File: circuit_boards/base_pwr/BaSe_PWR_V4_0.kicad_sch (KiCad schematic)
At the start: 107 parts, among them J1 12VDC In, J1 USB_C_Receptacle, J10 Conn_01x04_Socket, J11 MOTOR, J3 USB3_A, J3 USB_B_Micro, J4 Conn_01x07_Pin, J5 Conn_02x06_Odd_Even, J7 Conn_02x06_Odd_Even, J7 USB3_B_Micro, J9 Conn_01x04_Socket, P1 USB_C_Plug, Q1 AOSP21321, Q2 BSS214NW, Q3 BSS214NW, Q4 BSS214NW, Q5 BSS214NW, U1 STM32F070RBTx, U2 LM2596S-5, U3 AMS1117-3.3, U4 AMS1117-3.3, U5 DRV8220, U6 TS0101F020V4, Y1 8MHz

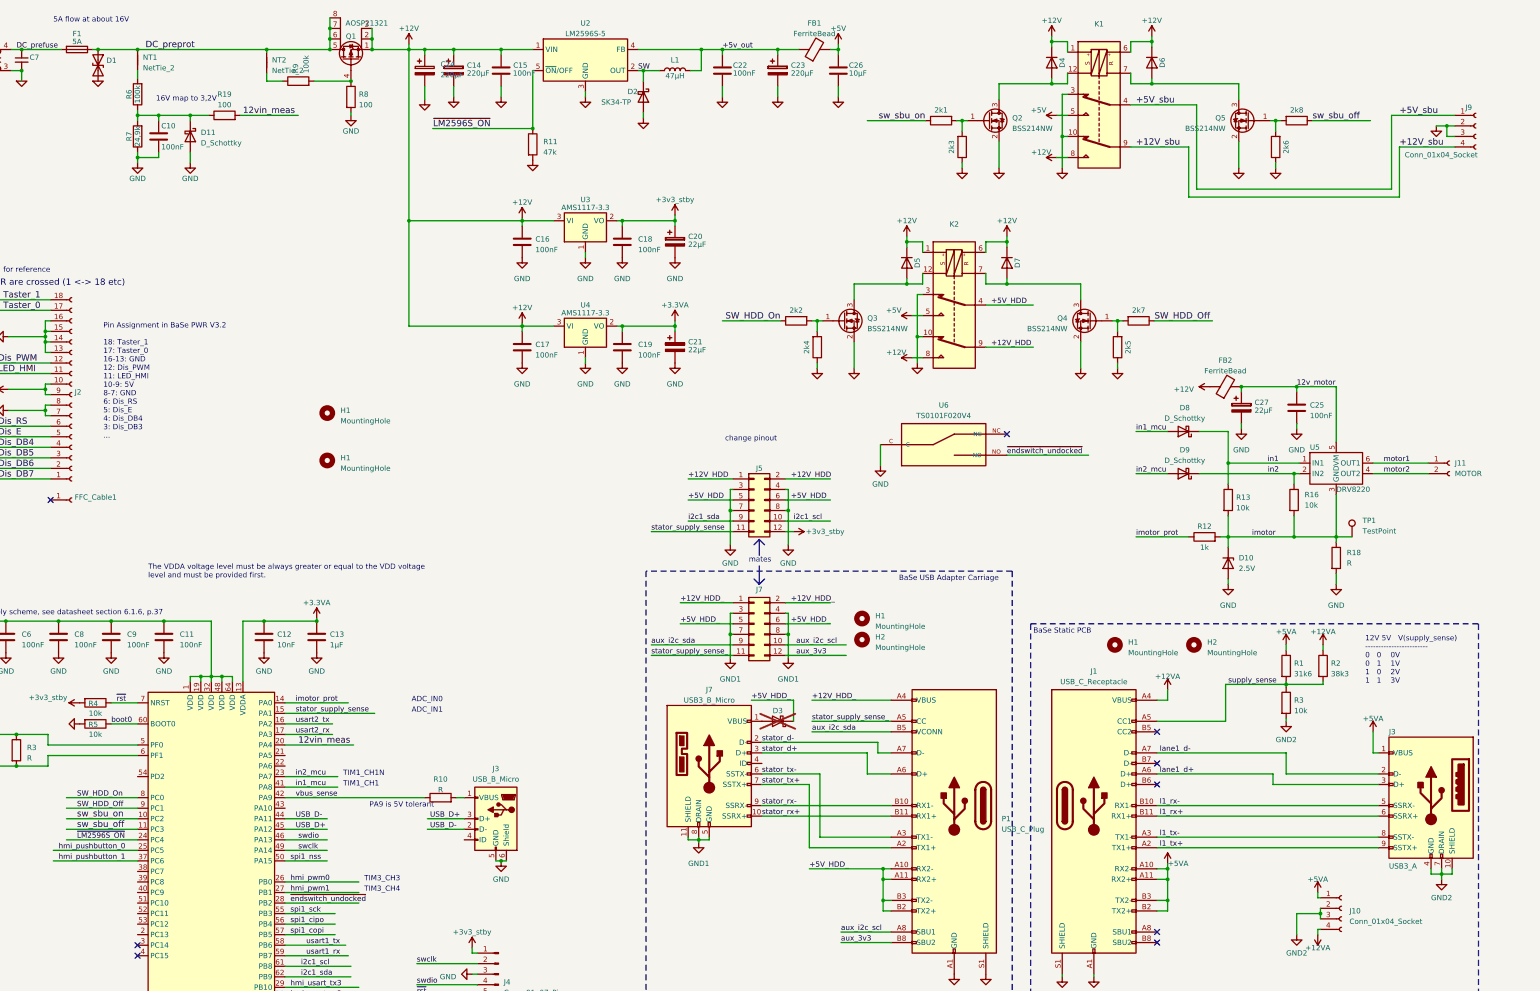
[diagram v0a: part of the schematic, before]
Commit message: update resistor values for supply sense
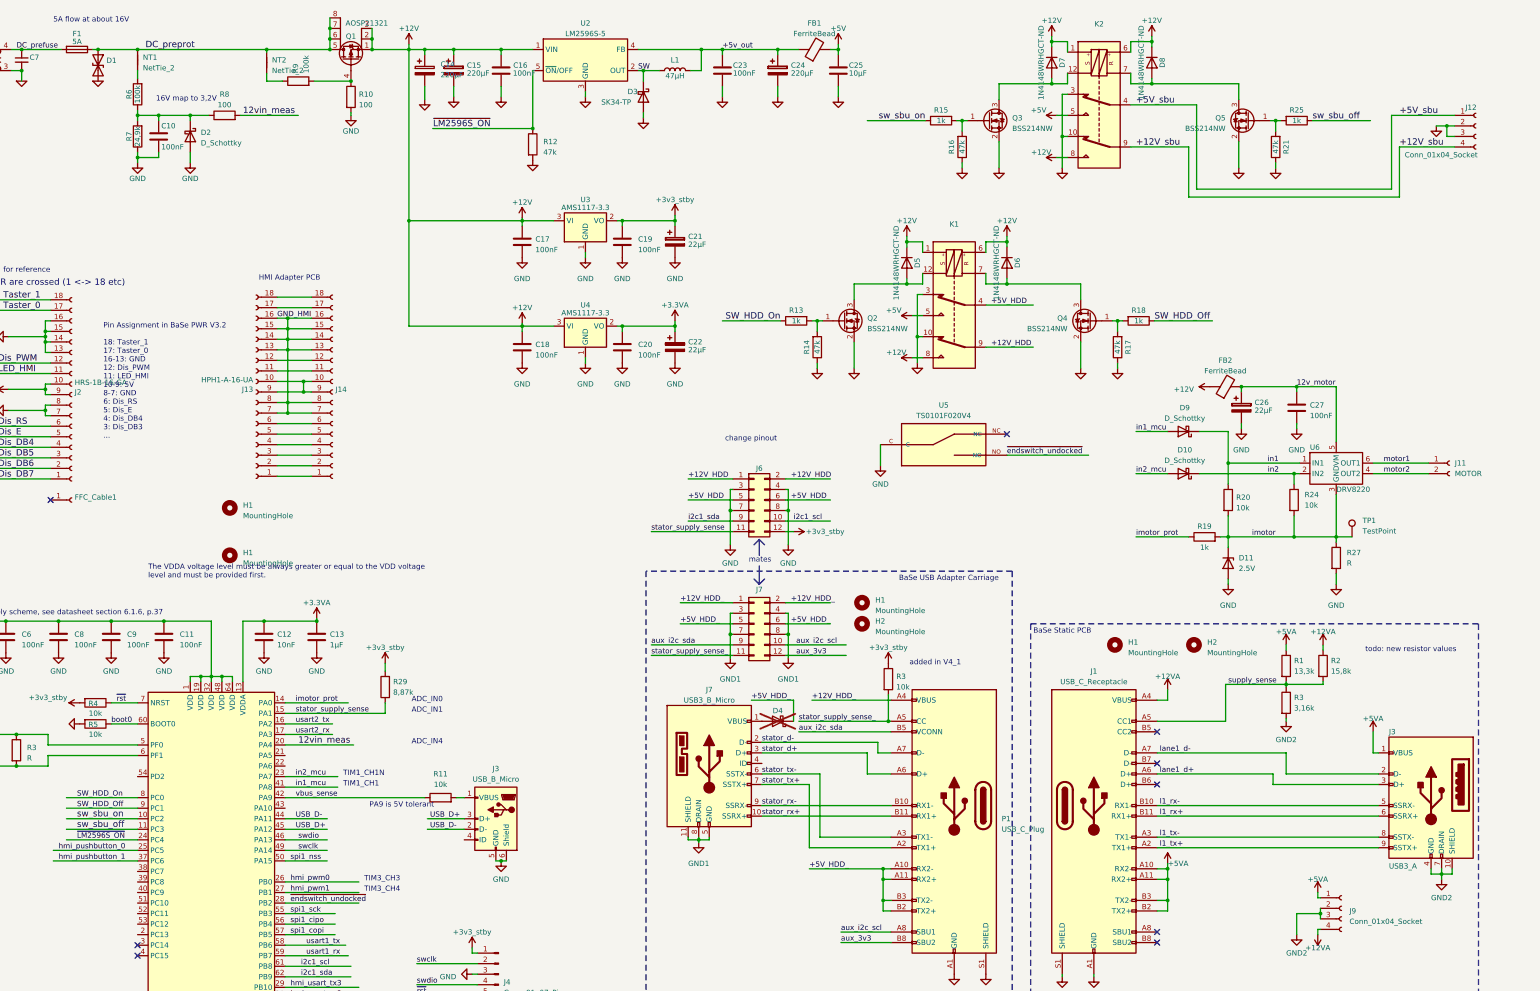
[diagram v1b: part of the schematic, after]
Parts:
- added J13: HPH1-A-16-UA, Connector_PinHeader_1.27mm:PinHeader_1x18_P1.27mm_Vertical, symbol Connector:Conn_01x18_Female
- added J14: ~, g7_connectors:molex_fcc_05220, symbol Connector:Conn_01x18_Female
- added R29: 8,87k, Resistor_SMD:R_0603_1608Metric_Pad0.98x0.95mm_HandSolder, symbol Device:R
- added R3: 10k, Resistor_SMD:R_0603_1608Metric_Pad0.98x0.95mm_HandSolder, symbol Device:R
- D5: value ~ -> 1N4148WRHGCT-ND
- D6: renamed from D7; value ~ -> 1N4148WRHGCT-ND
- D7: renamed from D4; value ~ -> 1N4148WRHGCT-ND
- D8: renamed from D6; value ~ -> 1N4148WRHGCT-ND
- J2: value ~ -> HRS-1B-16-GA; SPN WM10954CT-ND -> HRS-1B-16-GA
- R1: value 31k6 -> 13,3k
- R11: renamed from R10; value R -> 10k
- R13: renamed from 2k2; value ~ -> 1k
- R14: renamed from 2k4; value ~ -> 47k
- R15: renamed from 2k1; value ~ -> 1k
- R16: renamed from 2k3; value ~ -> 47k
- R17: renamed from 2k5; value ~ -> 47k
- R18: renamed from 2k7; value ~ -> 1k
- R2: value 38k3 -> 15,8k
- R21: renamed from 2k6; value ~ -> 47k
- R25: renamed from 2k8; value ~ -> 1k
- R3: value 10k -> 3,16k
- renumbered C24 to C14, C14 to C15, C15 to C16, C16 to C17, C17 to C18, C18 to C19, C19 to C20, C20 to C21, C21 to C22, C22 to C23, C23 to C24, C26 to C25, C27 to C26, C25 to C27, D9 to D10, D10 to D11, D11 to D2, D2 to D3, D3 to D4, D8 to D9, J9 to J12, J5 to J6, J10 to J9, K2 to K1, K1 to K2, Q3 to Q2, Q2 to Q3, R8 to R10, R11 to R12, R12 to R19, R13 to R20, R16 to R24, R18 to R27, R19 to R8, U6 to U5, U5 to U6
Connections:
- net +3V3_STBY: now also R29.2, R3.1
- net stator_supply_sense: now also R29.1
- net stator_supply_sense_: now also R3.2
- new net: J13.1 (Pin_1), J14.1 (Pin_1)
- new net: J13.10 (Pin_10), J13.9 (Pin_9), J14.10 (Pin_10), J14.9 (Pin_9)
- new net: J13.11 (Pin_11), J14.11 (Pin_11)
- new net: J13.12 (Pin_12), J14.12 (Pin_12)
- new net: J13.17 (Pin_17), J14.17 (Pin_17)
- new net: J13.18 (Pin_18), J14.18 (Pin_18)
- new net: J13.2 (Pin_2), J14.2 (Pin_2)
- new net: J13.3 (Pin_3), J14.3 (Pin_3)
- new net: J13.4 (Pin_4), J14.4 (Pin_4)
- new net: J13.5 (Pin_5), J14.5 (Pin_5)
- new net: J13.6 (Pin_6), J14.6 (Pin_6)
- new net GND_HMI: J13.13 (Pin_13), J13.14 (Pin_14), J13.15 (Pin_15), J13.16 (Pin_16), J13.7 (Pin_7), J13.8 (Pin_8), J14.13 (Pin_13), J14.14 (Pin_14), J14.15 (Pin_15), J14.16 (Pin_16), J14.7 (Pin_7), J14.8 (Pin_8)
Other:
- note added: "ADC_IN4"
- note added: "HMI Adapter PCB"
- note added: "added in V4_1"
- note added: "todo: new resistor values"
- note removed: "12V 5V V(supply_sense) ------------------------ 0 0 0V 0 1 1V 1 0 2V 1 1 3V"
- moved on the sheet: H1, H2

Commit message: bom changes after bringup
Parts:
- D10, D2, D9: value D_Schottky -> SD103CW-E3-08
- D11: value 2.5V -> MMSZ5222BS
- D4: value ~ -> SK64L-TPMSCT-ND
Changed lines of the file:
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@@
       (effects (font (size 1.27 1.27)) (justify left))
     )
-    (property "Value" "D_Schottky" (at 98.425 43.4975 90)
+    (property "Value" "SD103CW-E3-08" (at 98.425 43.4975 90)
       (effects (font (size 1.27 1.27)) (justify left))
     )
@@
       (effects (font (size 1.27 1.27)))
     )
-    (property "Value" "D_Schottky" (at 335.5975 109.855 0)
+    (property "Value" "SD103CW-E3-08" (at 335.5975 109.855 0)
       (effects (font (size 1.27 1.27)))
     )
@@
       (effects (font (size 1.27 1.27)))
     )
-    (property "Value" "D_Schottky" (at 335.5975 120.015 0)
+    (property "Value" "SD103CW-E3-08" (at 335.5975 120.015 0)
       (effects (font (size 1.27 1.27)))
     )
@@
       (effects (font (size 1.27 1.27)))
     )
-    (property "Value" "~" (at 237.49 179.705 0)
+    (property "Value" "SK64L-TPMSCT-ND" (at 237.49 179.705 0)
       (effects (font (size 1.27 1.27)))
     )
@@
       (effects (font (size 1.27 1.27)) (justify left))
     )
-    (property "Value" "2.5V" (at 348.615 146.0499 90)
+    (property "Value" "MMSZ5222BS" (at 348.615 146.0499 90)
       (effects (font (size 1.27 1.27)) (justify left))
     )
